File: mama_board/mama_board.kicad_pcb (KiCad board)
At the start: 4 copper layers, 80 x 86 mm, 115 parts, among them J1 Programming Header, J10 Conn_01x06_Female, J4 M80-5000642, J7 TEST_CONN, U1 LTC6269, U10 MCP2562-E/SN, U11 AS393P-E1, U12 AS393P-E1, U2 LD3985M47R_SOT23, U3 LT3014IS5#TRMPBF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

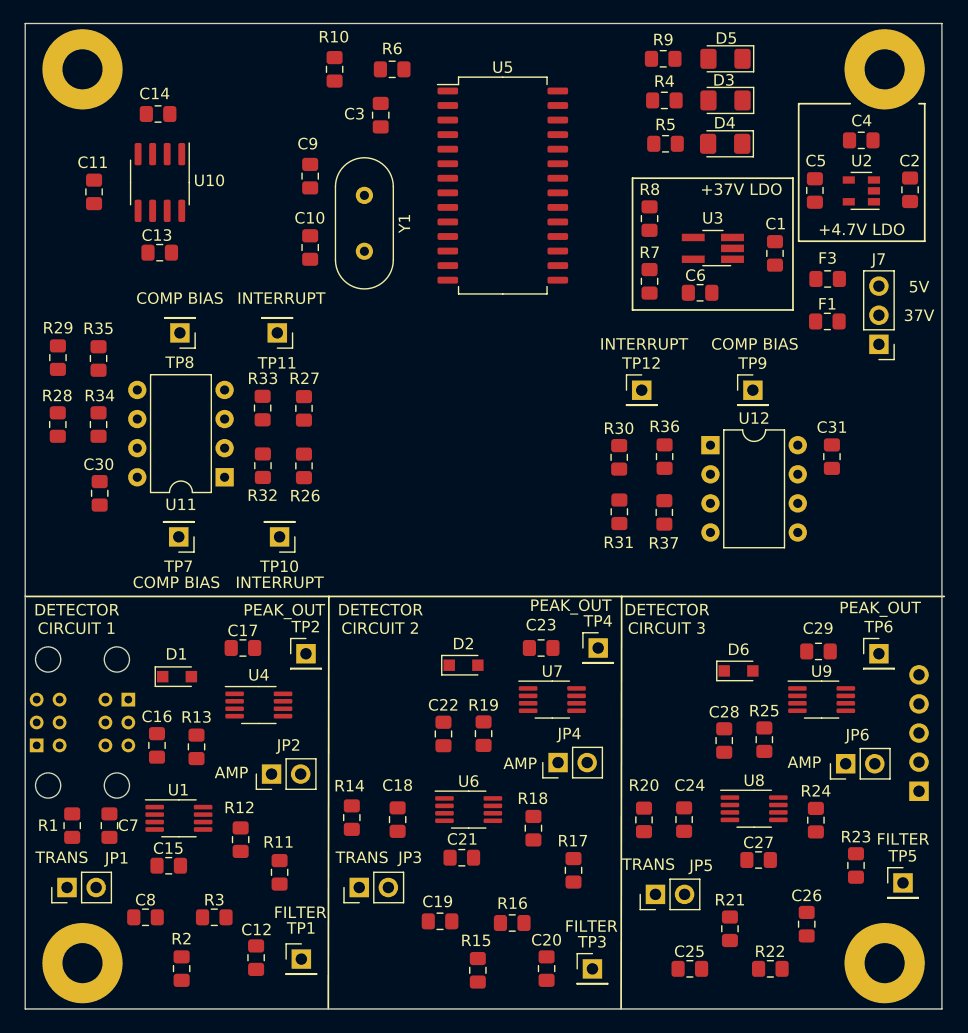
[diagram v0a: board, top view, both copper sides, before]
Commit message: Switch header positions
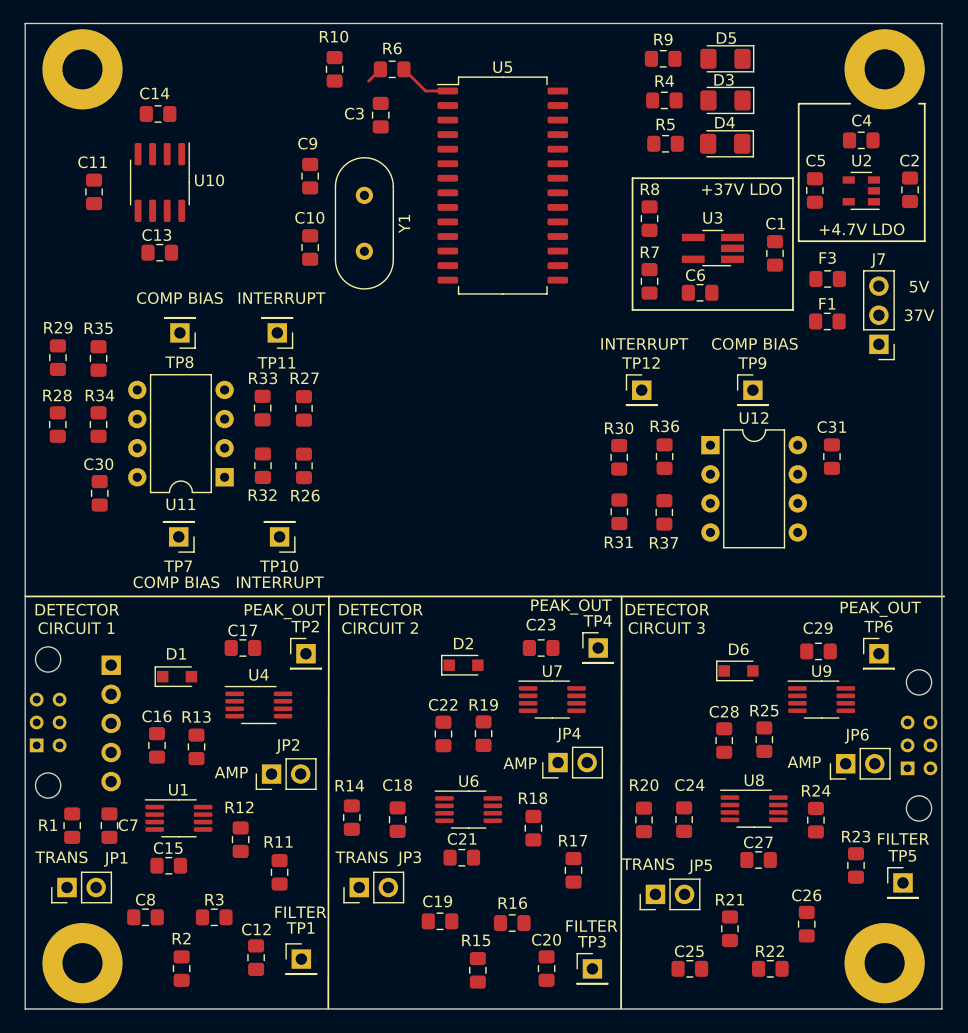
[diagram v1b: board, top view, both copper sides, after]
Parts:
- moved J1 71.4 mm to (115.5, 122.0), turned to 180 degrees
- moved J4 70.0 mm to (186.0, 129.0), turned to 90 degrees
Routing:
- net Net-(R6-Pad1): track 0.00 -> 4.61 mm
- net /Microcontroller [DO NOT PLACE]/MCLR: track 0.00 -> 1.45 mm

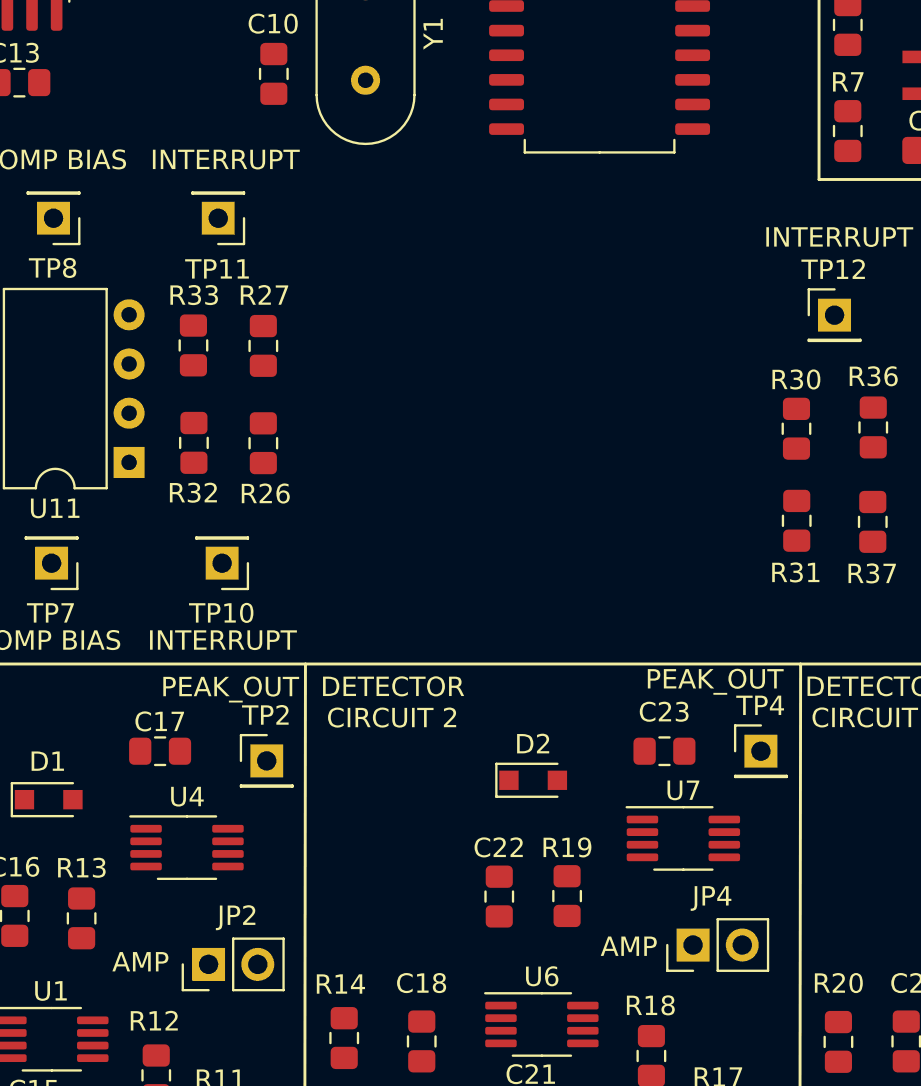
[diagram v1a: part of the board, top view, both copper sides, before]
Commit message: Add SiPM footprint, finish initial board layout
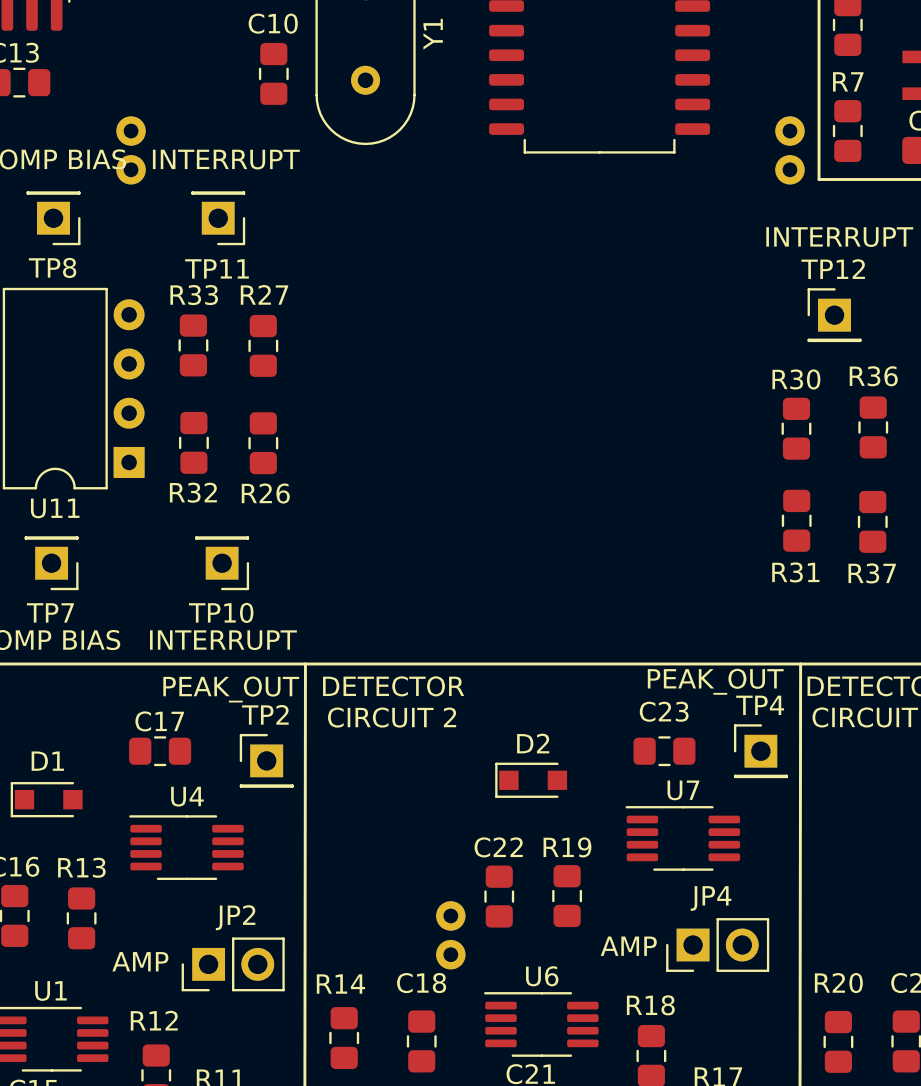
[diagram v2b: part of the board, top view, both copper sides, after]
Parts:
- added U13: Broadcom_SiPM_1, Payload2020_custom:BROADCOM_SiPM, B.Cu at (165.5, 87.0)
- added U14: Broadcom_SiPM_2, Payload2020_custom:BROADCOM_SiPM, B.Cu at (131.5, 87.0)
- added U15: Broadcom_SiPM_3, Payload2020_custom:BROADCOM_SiPM, B.Cu at (148.0, 127.5)

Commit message: Route components - 1/2 board complete
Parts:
- moved U14 34.2 mm to (165.7, 87.1)
- moved U13 34.0 mm to (131.5, 87.1)
- moved D5 8.70 mm to (170.1, 77.7)
- moved R9 8.70 mm to (164.7, 77.7)
- moved R5 6.68 mm to (164.9, 69.9)
- moved D4 6.68 mm to (170.1, 69.9)
- moved C17 2.67 mm to (129.5, 121.3)
- moved C10 2.60 mm to (132.8, 88.1)
- moved R17 2.31 mm to (154.4, 141.7)
- moved C23 2.02 mm to (154.9, 121.2)
- moved C27 1.56 mm to (170.5, 138.4)
- moved D3 1.44 mm to (170.1, 73.7)
- moved R4 1.44 mm to (164.8, 73.7)
- moved R23 1.39 mm to (179.3, 140.2)
- moved C29 1.33 mm to (178.6, 120.9)
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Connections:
- net /Microcontroller [DO NOT PLACE]/CANH renamed /Microcontroller/+
- net /Microcontroller [DO NOT PLACE]/CANL renamed /Microcontroller/-
- net /Microcontroller [DO NOT PLACE]/ICSPCLK renamed /Microcontroller/ICSPCLK
- net /Microcontroller [DO NOT PLACE]/ICSPDAT renamed /Microcontroller/ICSPDAT
- net /Microcontroller [DO NOT PLACE]/MCLR renamed /Microcontroller/MCLR
- net /Microcontroller [DO NOT PLACE]/OSC1 renamed /Microcontroller/OSC1
- net /Microcontroller [DO NOT PLACE]/OSC2 renamed /Microcontroller/OSC2
- net /Microcontroller [DO NOT PLACE]/PIC_RX renamed /Microcontroller/PIC_RX
- net /Microcontroller [DO NOT PLACE]/PIC_TX renamed /Microcontroller/PIC_TX
- U5 pad 2: /Comparitor Circuits/INTERRUPT_1 -> /Comparitor Circuits/INTERRUPT_3
- U5 pad 3: /Comparitor Circuits/INTERRUPT_2 -> /Comparitor Circuits/INTERRUPT_1
- U5 pad 4: /Comparitor Circuits/INTERRUPT_3 -> /Comparitor Circuits/INTERRUPT_2
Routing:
- net /Microcontroller/ICSPCLK: track 0.00 -> 98.1 mm, vias 0 -> 1
- net /Microcontroller/ICSPDAT: track 0.00 -> 96.2 mm, vias 0 -> 1
- net GND: track 0.00 -> 84.0 mm, vias 0 -> 30
- net /Microcontroller/MCLR: track 1.45 -> 77.7 mm, vias 0 -> 1
- net /Comparitor Circuits/INTERRUPT_1: track 0.00 -> 70.1 mm
- net /Microcontroller/+: track 0.00 -> 69.9 mm, vias 0 -> 1
- net /Microcontroller/-: track 0.00 -> 69.5 mm, vias 0 -> 1
- net /DET_ADC_3: track 0.00 -> 64.1 mm
- net /Comparitor Circuits/INTERRUPT_3: track 0.00 -> 60.4 mm
- net /AMP_OUT_2: track 0.00 -> 60.3 mm, vias 0 -> 1
- net /Comparitor Circuits/INTERRUPT_2: track 0.00 -> 58.2 mm
- net /DET_ADC_1: track 0.00 -> 53.1 mm
- net /DET_ADC_2: track 0.00 -> 45.5 mm
- net /AMP_OUT_1: track 0.00 -> 39.4 mm, vias 0 -> 1
- net +4.7V: track 0.00 -> 37.2 mm, vias 0 -> 6
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- added copper zone on VCC.Cu, net +4.7V
- added copper zone on B.Cu, net +5V
- added copper zone on F.Cu, net +5V
- added copper zone on F.Cu, net /Detector Circuit 1/SIPM_OUT_1
- added copper zone on F.Cu, net /Detector Circuit 2/SIPM_OUT_2
- added copper zone on F.Cu, net GND
- added copper zone on GND.Cu, net GND
- added copper zone on F.Cu, net Net-(C18-Pad1)
- added copper zone on F.Cu, net Net-(C24-Pad1)
- added copper zone on F.Cu, net Net-(C7-Pad1)

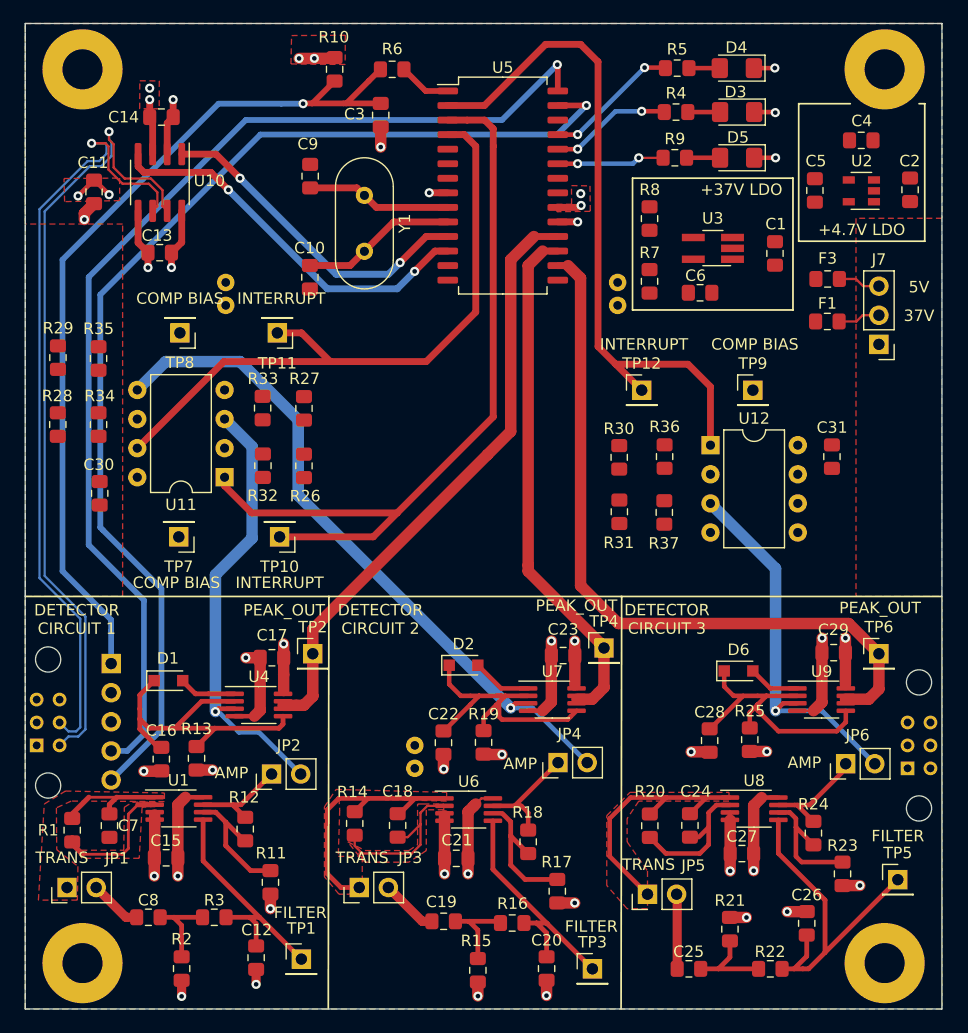
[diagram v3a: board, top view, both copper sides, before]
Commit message: Finish routing, still need to fix DRC errors
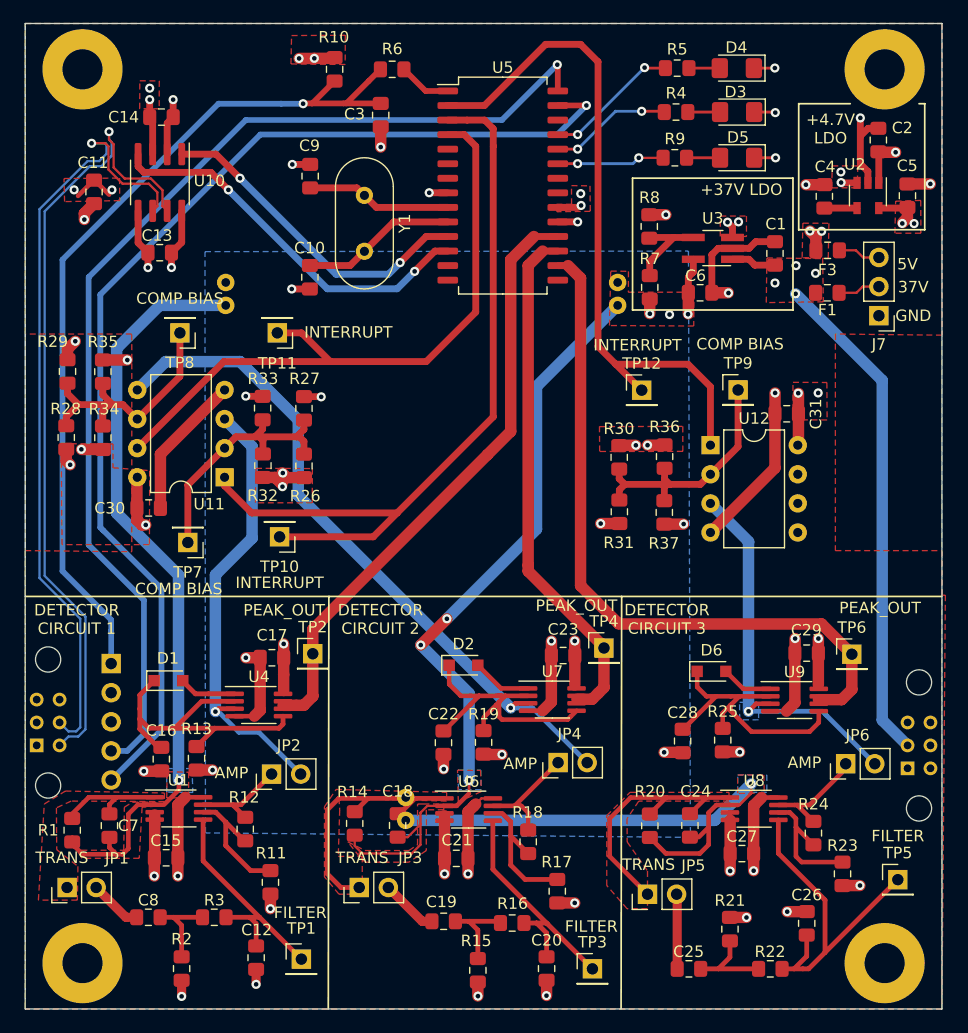
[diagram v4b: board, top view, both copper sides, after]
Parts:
- moved C5 8.09 mm to (185.0, 81.0)
- moved C4 5.85 mm to (177.7, 81.1), turned to 90 degrees
- moved C31 5.44 mm to (174.5, 100.1), turned to 180 degrees
- moved C2 5.15 mm to (182.4, 76.2)
- moved U15 4.61 mm to (147.2, 132.0)
- moved C30 4.46 mm to (118.8, 108.3), turned to 0 degrees
- moved F1 2.50 mm to (178.0, 89.5)
- moved F3 2.50 mm to (178.0, 85.8)
- moved J7 2.50 mm to (182.5, 91.5)
- moved D6 2.36 mm to (167.9, 122.5)
- moved TP6 2.36 mm to (180.1, 121.0)
- moved U9 2.36 mm to (175.1, 125.0)
- moved C28 2.36 mm to (165.4, 128.6)
- moved C29 2.36 mm to (176.2, 120.9)
- moved R25 2.36 mm to (168.9, 128.5)
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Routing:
- net GND: track 84.0 -> 148.3 mm, vias 30 -> 44
- net /Detector Circuit 1/SIPM_OUT_1: track 13.2 -> 69.4 mm, vias 0 -> 1
- net /Detector Circuit 2/SIPM_OUT_2: track 15.3 -> 69.4 mm, vias 0 -> 3
- net +37V: track 0.00 -> 49.4 mm, vias 0 -> 4
- net /Detector Circuit 3/SIPM_OUT_3: track 13.1 -> 47.7 mm, vias 0 -> 1
- net Net-(R28-Pad2): track 0.00 -> 23.6 mm
- net Net-(R26-Pad2): track 0.00 -> 23.3 mm
- net +5V: track 18.9 -> 41.9 mm, vias 9 -> 22
- net Net-(R30-Pad2): track 0.00 -> 22.4 mm
- net +4.7V: track 37.2 -> 46.9 mm, vias 6 -> 11
- net Net-(R7-Pad2): track 0.00 -> 8.06 mm
- net +36V: track 0.00 -> 6.27 mm, vias 0 -> 3
- net Net-(C4-Pad1): track 0.00 -> 2.85 mm
- net /DET_ADC_3: track 64.1 -> 61.8 mm
- net /AMP_OUT_3: track 33.2 -> 34.6 mm
- added copper zone on B.Cu, net +36V
- added copper zone on F.Cu, net +36V
- added copper zone on F.Cu, net +37V
- added copper zone on F.Cu, net +4.7V
- added copper zone on VCC.Cu, net +5V
- added copper zone on B.Cu, net /AMP_OUT_3
- added copper zone on B.Cu, net /Detector Circuit 1/SIPM_OUT_1
- added copper zone on B.Cu, net /Detector Circuit 2/SIPM_OUT_2
- added copper zone on B.Cu, net /Detector Circuit 3/SIPM_OUT_3
- added copper zone on F.Cu, net /Detector Circuit 3/SIPM_OUT_3
- added copper zone on B.Cu, net GND
- removed copper zone on B.Cu, net +5V

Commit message: Fix DRC errors, finish silkscreen, update schematic pdf
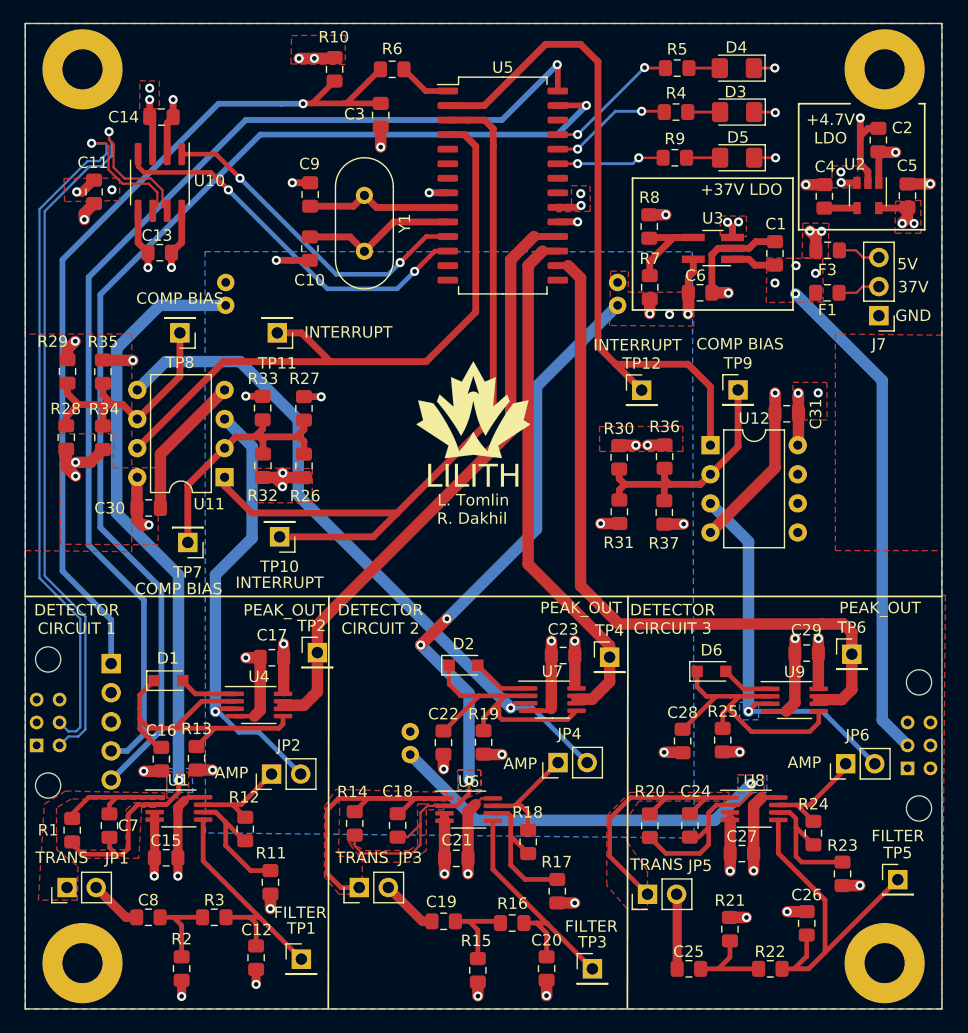
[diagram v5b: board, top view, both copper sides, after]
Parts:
- added G***: LOGO, Payload2020_custom:Logo_SilkScreen_10mm, F.Cu at (147.1, 99.7)
- moved U15 5.75 mm to (147.6, 126.3)
- moved C10 2.50 mm to (132.8, 85.6)
- moved C9 1.60 mm to (132.9, 80.9)
- moved TP4 0.94 mm to (159.0, 121.3)
- moved TP2 0.42 mm to (133.5, 120.9)
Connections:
- net /Microcontroller/+ renamed /Microcontroller/CANH
- net /Microcontroller/- renamed /Microcontroller/CANL
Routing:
- net GND: track 148.3 -> 151.7 mm
- net /Detector Circuit 3/SIPM_OUT_3: track 47.7 -> 49.7 mm
- net /Detector Circuit 1/SIPM_OUT_1: track 69.4 -> 71.2 mm
- net /DET_ADC_3: track 61.8 -> 62.9 mm
- net Net-(R17-Pad1): track 12.4 -> 13.5 mm
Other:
- board text added: "L. Tomlin"
- board text added: "LILITH"
- board text added: "R. Dakhil"
